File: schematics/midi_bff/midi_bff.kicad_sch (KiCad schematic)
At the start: 17 parts, among them CN1 DIN-504, CN2 DIN-504, J1 PJ-320A-4P DIP, J2 PJ-320A-4P DIP, U3 H11L1

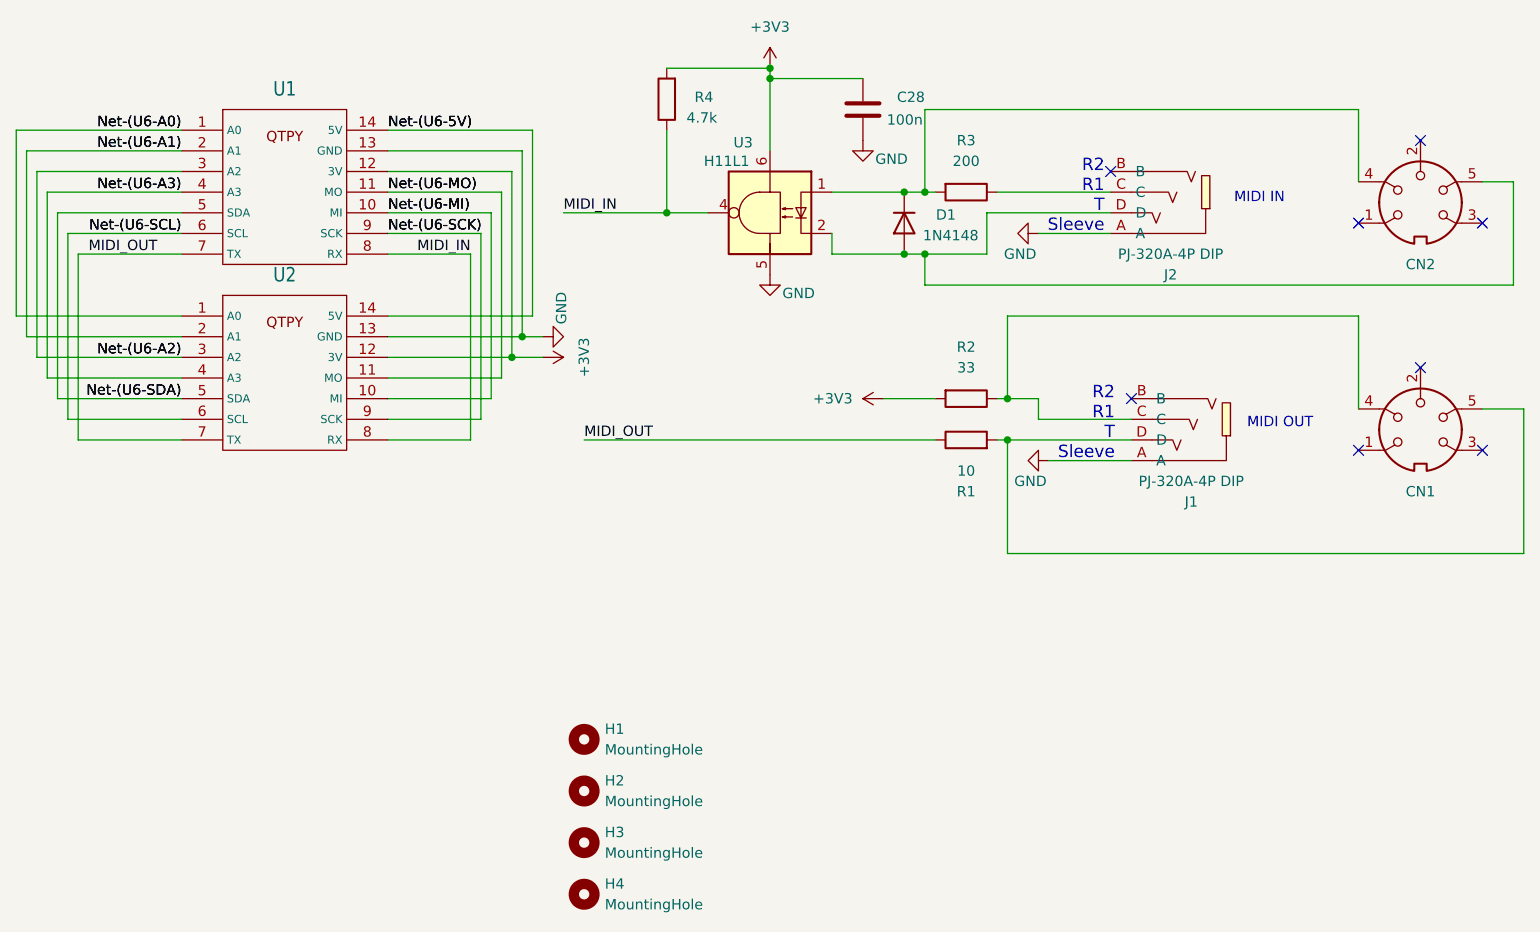
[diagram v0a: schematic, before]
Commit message: sent to production
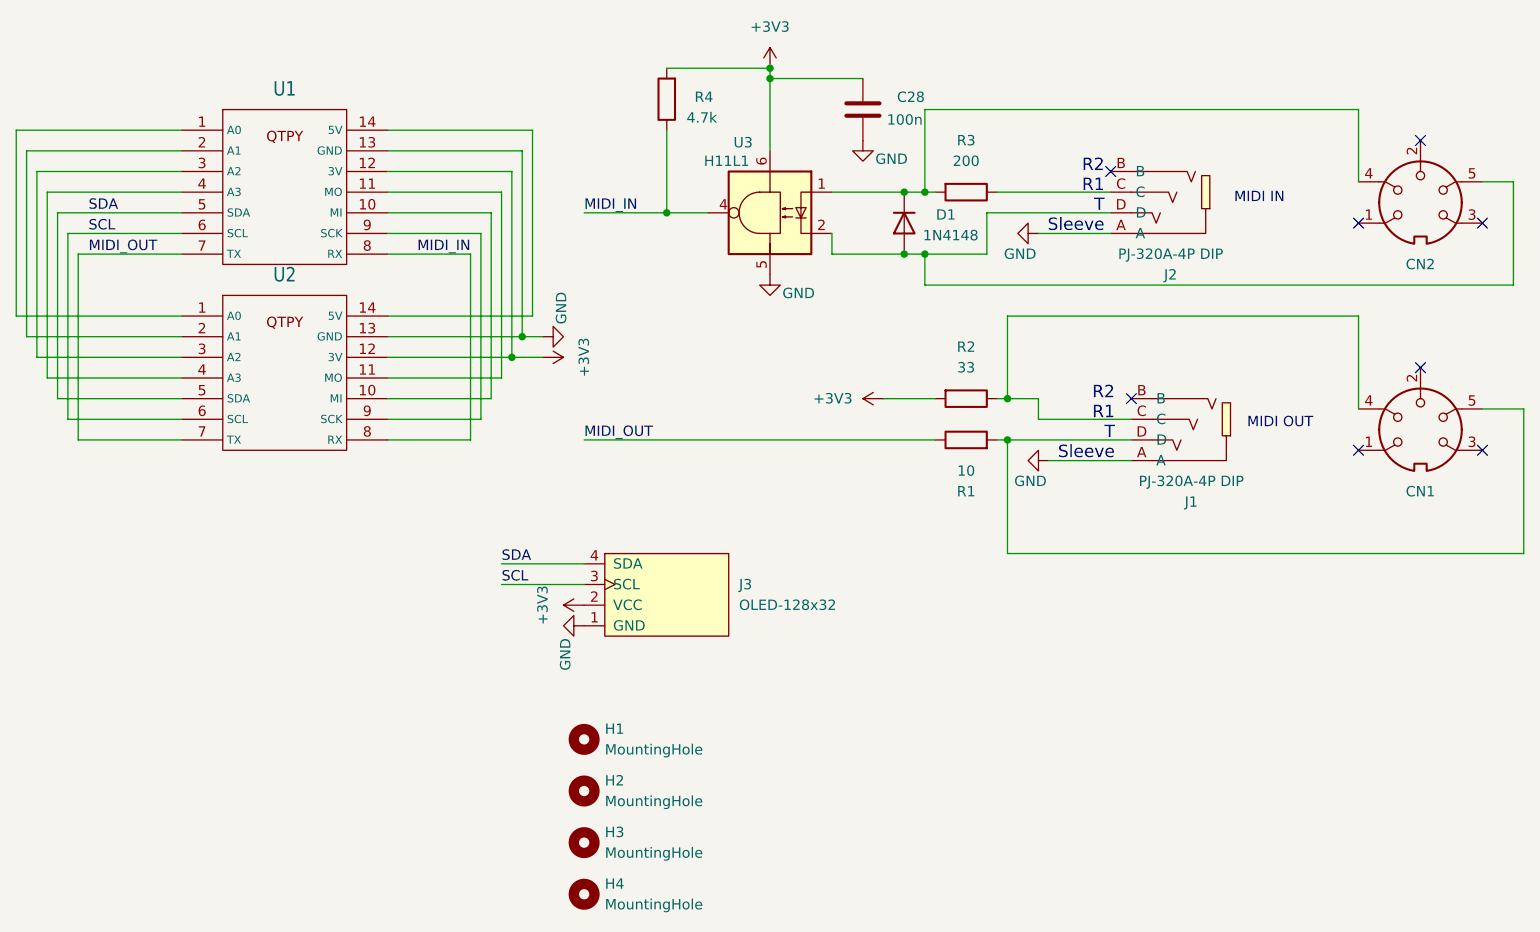
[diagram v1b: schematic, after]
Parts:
- added J3: OLED-128x32, kleeb-display:OLED-128x32, symbol kleeb-display:OLED-128x32
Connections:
- net +3V3: now also J3.2 (VCC)
- net GND: now also J3.1 (GND)
- net Net-(U6-5V): no longer names the net of U1.14 (5V), U2.14 (5V)
- net Net-(U6-A0): no longer names the net of U1.1 (A0), U2.1 (A0)
- net Net-(U6-A1): no longer names the net of U1.2 (A1), U2.2 (A1)
- net Net-(U6-A2): no longer names the net of U1.3 (A2), U2.3 (A2)
- net Net-(U6-A3): no longer names the net of U1.4 (A3), U2.4 (A3)
- net Net-(U6-MI): no longer names the net of U1.10 (MI), U2.10 (MI)
- net Net-(U6-MO): no longer names the net of U1.11 (MO), U2.11 (MO)
- net Net-(U6-SCK): no longer names the net of U1.9 (SCK), U2.9 (SCK)
- net Net-(U6-SCL) renamed SCL
- net SCL: now also J3.3 (SCL)
- net Net-(U6-SDA) renamed SDA
- net SDA: now also J3.4 (SDA)
